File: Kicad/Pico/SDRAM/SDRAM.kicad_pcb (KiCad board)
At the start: 2 copper layers, 68.3 x 73.7 mm, 17 parts, among them IC1 AS4C32M8SA-6TIN, IC3 74LVC574APW,118, IC4 74LVC574APW,118, J1 Conn_01x03_Pin, J4 Conn_01x03_Pin, J5 Conn_01x20_Pin, J6 Conn_01x20_Pin

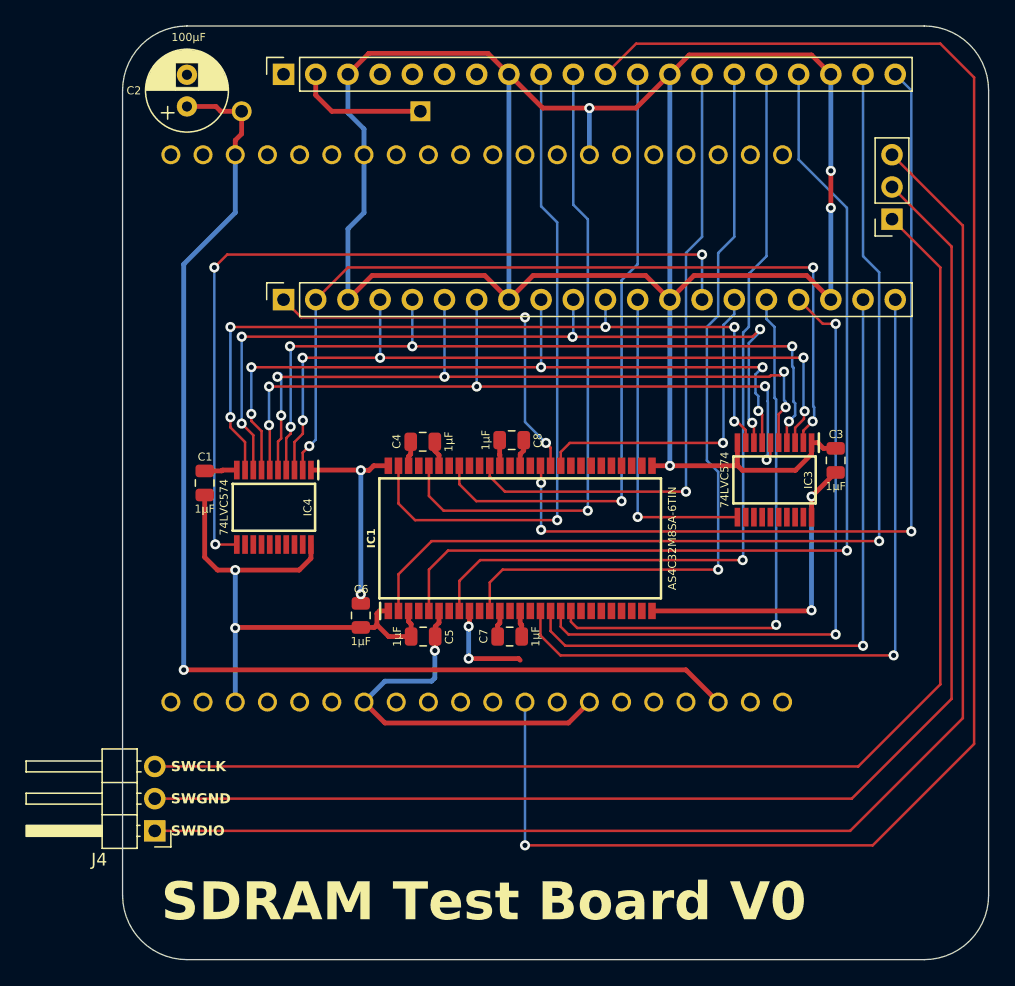
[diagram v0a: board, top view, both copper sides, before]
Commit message: Route SDRAM test board.
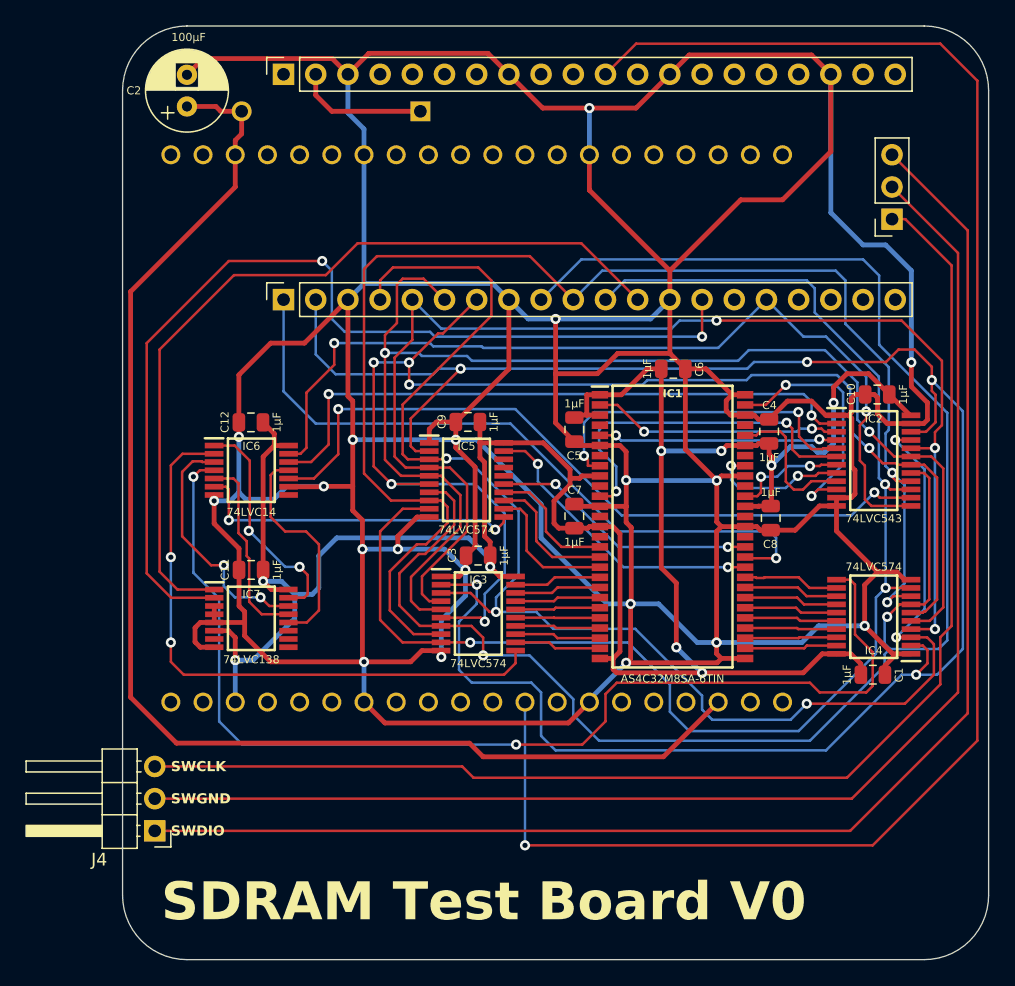
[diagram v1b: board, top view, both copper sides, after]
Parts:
- added C10: 1μF, SamacSys_Parts:C_0805, F.Cu at (55.7, -26.8)
- added C11: 1μF, SamacSys_Parts:C_0805, F.Cu at (6.34, -13.0)
- added C12: 1μF, SamacSys_Parts:C_0805, F.Cu at (6.33, -24.6)
- added C9: 1μF, SamacSys_Parts:C_0805, F.Cu at (23.4, -24.6)
- added IC2: SN74LVC543APWR, SamacSys_Parts:SOP65P640X120-24N, F.Cu at (55.5, -21.6)
- added IC5: 74LVC574APW,118, SamacSys_Parts:SOP65P640X110-20N, F.Cu at (23.3, -20.1)
- added IC6: 74LVC14APW,118, SamacSys_Parts:SOP65P640X110-14N, F.Cu at (6.35, -20.8)
- added IC7: 74LVC138APW-Q100J, SamacSys_Parts:SOP65P640X110-16N, F.Cu at (6.35, -9.14)
- moved C1 54.8 mm to (55.4, -4.70), turned to -90 degrees
- moved IC4 48.1 mm to (55.5, -9.27), turned to 180 degrees
- moved C6 31.4 mm to (39.6, -28.8), turned to -90 degrees
- moved C3 29.2 mm to (24.3, -14.1), turned to 90 degrees
- moved C4 27.3 mm to (47.2, -23.9), turned to 0 degrees
- moved IC3 25.6 mm to (24.3, -9.53), turned to 0 degrees
- moved C8 21.4 mm to (47.3, -17.1), turned to 180 degrees
- moved C5 20.2 mm to (31.8, -24.1), turned to 180 degrees
- moved IC1 12.1 mm to (39.6, -16.4), turned to 0 degrees
- moved C7 10.8 mm to (31.8, -17.2), turned to 0 degrees
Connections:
- IC3 pad 11: /CP1 -> /Y0
- IC3 pad 12: /BA1 -> /A3
- IC3 pad 13: /BA0 -> /A2
- IC3 pad 14: unconnected-(IC3-Q5-Pad14) -> /A1
- IC3 pad 15: /A12 -> /A0
- IC3 pad 16: /A11 -> /A10
- IC3 pad 17: /A10 -> /BA1
- IC3 pad 18: /A9 -> /BA0
- IC3 pad 19: /A8 -> /~{CS}
- IC4 pad 11: /CP2 -> /Y1
- IC4 pad 12: /A7 -> /A12
- IC4 pad 13: /A6 -> /A11
- IC4 pad 14: /A5 -> /A9
- IC4 pad 15: /A4 -> /A8
- IC4 pad 16: /A3 -> /A7
- IC4 pad 17: /A2 -> /A6
- IC4 pad 18: /A1 -> /A5
- IC4 pad 19: /A0 -> /A4
- J5 pad 12: /CP1 -> /GA0
- J5 pad 14: /CP2 -> /GA1
- J5 pad 15: /CKE -> unconnected-(J5-Pin_15-Pad15)
- J5 pad 16: /~{CS} -> /AB
- J5 pad 17: /~{RAS} -> unconnected-(J5-Pin_17-Pad17)
- J5 pad 18: /GND -> unconnected-(J5-Pin_18-Pad18)
- J5 pad 19: /~{CAS} -> unconnected-(J5-Pin_19-Pad19)
- J5 pad 20: /~{WE} -> unconnected-(J5-Pin_20-Pad20)
- J6 pad 10: /D6 -> unconnected-(J6-Pin_10-Pad10)
- J6 pad 12: /D5 -> unconnected-(J6-Pin_12-Pad12)
- J6 pad 14: /D4 -> unconnected-(J6-Pin_14-Pad14)
- J6 pad 15: /D3 -> unconnected-(J6-Pin_15-Pad15)
- J6 pad 16: /D2 -> unconnected-(J6-Pin_16-Pad16)
- J6 pad 17: /D1 -> unconnected-(J6-Pin_17-Pad17)
- J6 pad 19: /D0 -> unconnected-(J6-Pin_19-Pad19)
- J6 pad 20: /DQM -> unconnected-(J6-Pin_20-Pad20)
- J6 pad 9: /D7 -> unconnected-(J6-Pin_9-Pad9)
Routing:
- net /GND: track 249.3 -> 562.5 mm, vias 7 -> 19
- net /3.3V: track 83.9 -> 192.8 mm, vias 6 -> 9
- net /Y1: track 0.00 -> 88.3 mm, vias 0 -> 2
- net /GP0: track 68.4 -> 154.9 mm, vias 3 -> 5
- net /GP5: track 60.5 -> 143.0 mm, vias 5 -> 2
- net /GA1: track 0.00 -> 78.4 mm, vias 0 -> 2
- net /AB: track 0.00 -> 70.9 mm, vias 0 -> 2
- net /CP2: track 66.0 -> 0.00 mm, vias 3 -> 0
- net /GA0: track 0.00 -> 65.5 mm
- net /D0: track 79.3 -> 19.7 mm, vias 1 -> 2
- net /Y3: track 0.00 -> 57.9 mm, vias 0 -> 2
- net /D1: track 76.0 -> 18.9 mm, vias 1 -> 2
- net /GP1: track 60.3 -> 117.0 mm
- net /DQM: track 70.9 -> 21.1 mm, vias 3 -> 2
- net /BA: track 0.00 -> 49.4 mm, vias 0 -> 2
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
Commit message: Cleaned SDRAM Tester schematic.
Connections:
- J5 pad 15: unconnected-(J5-Pin_15-Pad15) -> /AB
- J5 pad 16: /AB -> unconnected-(J5-Pin_16-Pad16)
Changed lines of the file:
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@@
 			(layers "*.Cu" "*.Mask")
 			(remove_unused_layers no)
-			(net "unconnected-(J5-Pin_15-Pad15)")
+			(net "/AB")
 			(pinfunction "Pin_15_15")
-			(pintype "passive+no_connect")
+			(pintype "passive")
 		)
 		(pad "16" thru_hole circle
@@
 			(layers "*.Cu" "*.Mask")
 			(remove_unused_layers no)
-			(net "/AB")
+			(net "unconnected-(J5-Pin_16-Pad16)")
 			(pinfunction "Pin_16_16")
-			(pintype "passive")
+			(pintype "passive+no_connect")
 		)
 		(pad "17" thru_hole circle
@@
 	)
 	(segment
-		(start 43.18 -30.48)
-		(end 46.99 -34.29)
-		(width 0.2)
-		(layer "B.Cu")
-		(net "/AB")
-	)
-	(segment
 		(start 54.8588 -28.1992)
 		(end 51.689 -31.369)
@@
 	)
 	(segment
-		(start 20.447 -30.861)
-		(end 20.701 -30.607)
+		(start 51.308 -31.75)
+		(end 51.689 -31.369)
 		(width 0.2)
 		(layer "B.Cu")
@@
 	)
 	(segment
-		(start 51.689 -31.369)
-		(end 49.911 -31.369)
+		(start 44.45 -31.75)
+		(end 51.308 -31.75)
 		(width 0.2)
 		(layer "B.Cu")
@@
 	)
 	(segment
-		(start 12.8905 -30.861)
-		(end 20.447 -30.861)
+		(start 44.45 -31.75)
+		(end 44.45 -34.29)
 		(width 0.2)
 		(layer "B.Cu")
@@
 	)
 	(segment
+		(start 24.638 -30.48)
+		(end 43.18 -30.48)
+		(width 0.2)
+		(layer "B.Cu")
+		(net "/AB")
+	)
+	(segment
 		(start 54.8588 -25.4711)
 		(end 54.8588 -28.1992)
@@
 	)
 	(segment
-		(start 49.911 -31.369)
-		(end 46.99 -34.29)
+		(start 20.447 -30.861)
+		(end 20.701 -30.607)
 		(width 0.2)
 		(layer "B.Cu")
@@
 	)
 	(segment
-		(start 24.638 -30.48)
-		(end 43.18 -30.48)
+		(start 12.8905 -30.861)
+		(end 20.447 -30.861)
+		(width 0.2)
+		(layer "B.Cu")
+		(net "/AB")
+	)
+	(segment
+		(start 43.18 -30.48)
+		(end 44.45 -31.75)
 		(width 0.2)
 		(layer "B.Cu")

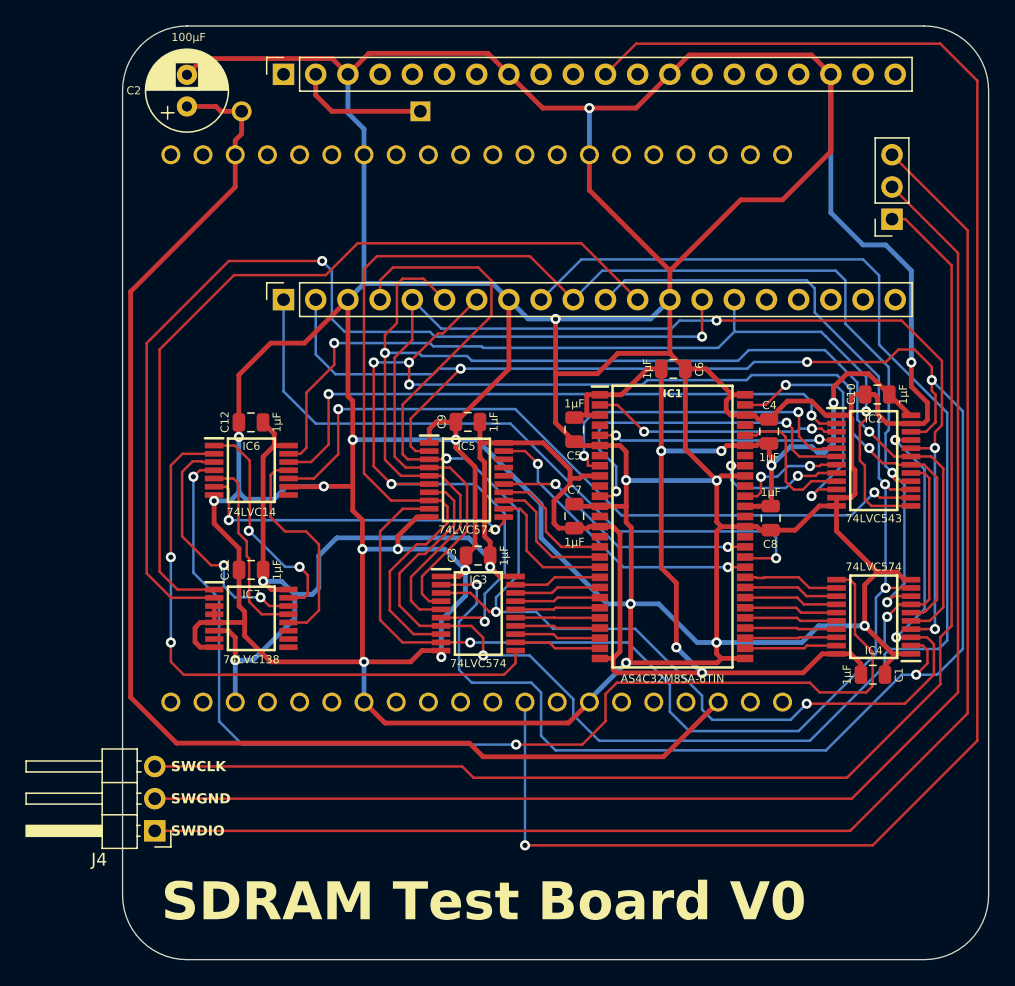
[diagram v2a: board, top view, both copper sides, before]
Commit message: Cleaned SDRAM routing.
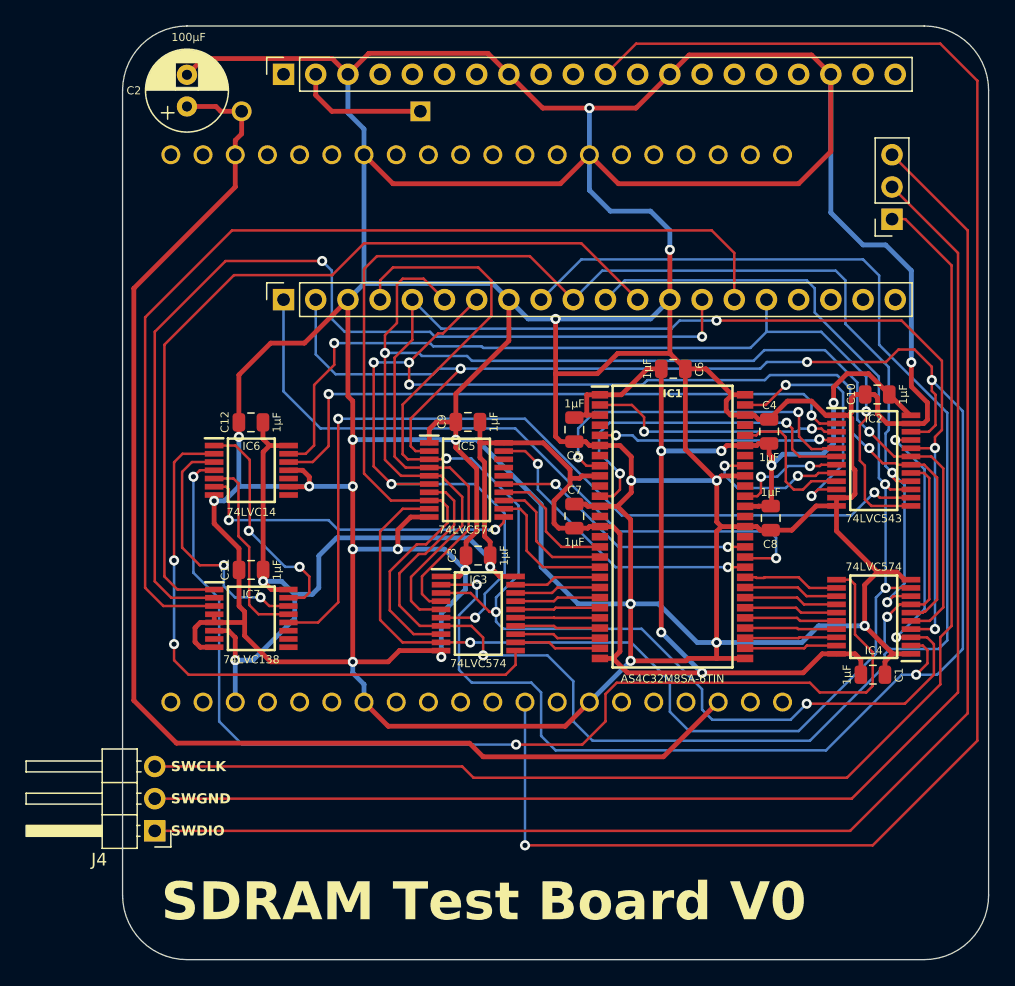
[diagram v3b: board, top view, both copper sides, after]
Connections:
- IC2 pad 14: /Y3 -> /~{Y3}
- IC6 pad 10: /Y3 -> unconnected-(IC6-5Y-Pad10)
- IC6 pad 11: /~{Y3} -> /GND
- IC7 pad 3: /GND -> /GA2
- J5 pad 15: /AB -> /GA2
- J5 pad 16: unconnected-(J5-Pin_16-Pad16) -> /AB
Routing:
- net /GA2: track 0.00 -> 81.1 mm
- net /Y3: track 57.9 -> 0.00 mm, vias 2 -> 0
- net /~{Y3}: track 17.6 -> 68.3 mm, vias 0 -> 2
- net /GND: track 562.5 -> 590.8 mm, vias 19 -> 21
- net /GP5: track 143.0 -> 144.1 mm
- net /GP1: track 117.0 -> 117.9 mm
- net /GP4: track 107.2 -> 106.3 mm
- net /D5: track 11.3 -> 12.1 mm
- net /D0: track 19.7 -> 20.4 mm
- net /3.3V: track 192.8 -> 192.2 mm
